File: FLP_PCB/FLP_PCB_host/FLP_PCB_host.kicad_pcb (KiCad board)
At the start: 2 copper layers, 90 x 90.5 mm, 91 parts, among them J3 GRPB052VWVN-RC, J4 OLED, J5 SMA-J-P-X-ST-TH1, Q1 Q_PMOS_DSG, Q2 UMH3N, U1 ESP32-WROOM-32E, U2 TPS61200DRC, U3 MCP73831-2-OT, U4 AMS1117-3.3, U5 CP2104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

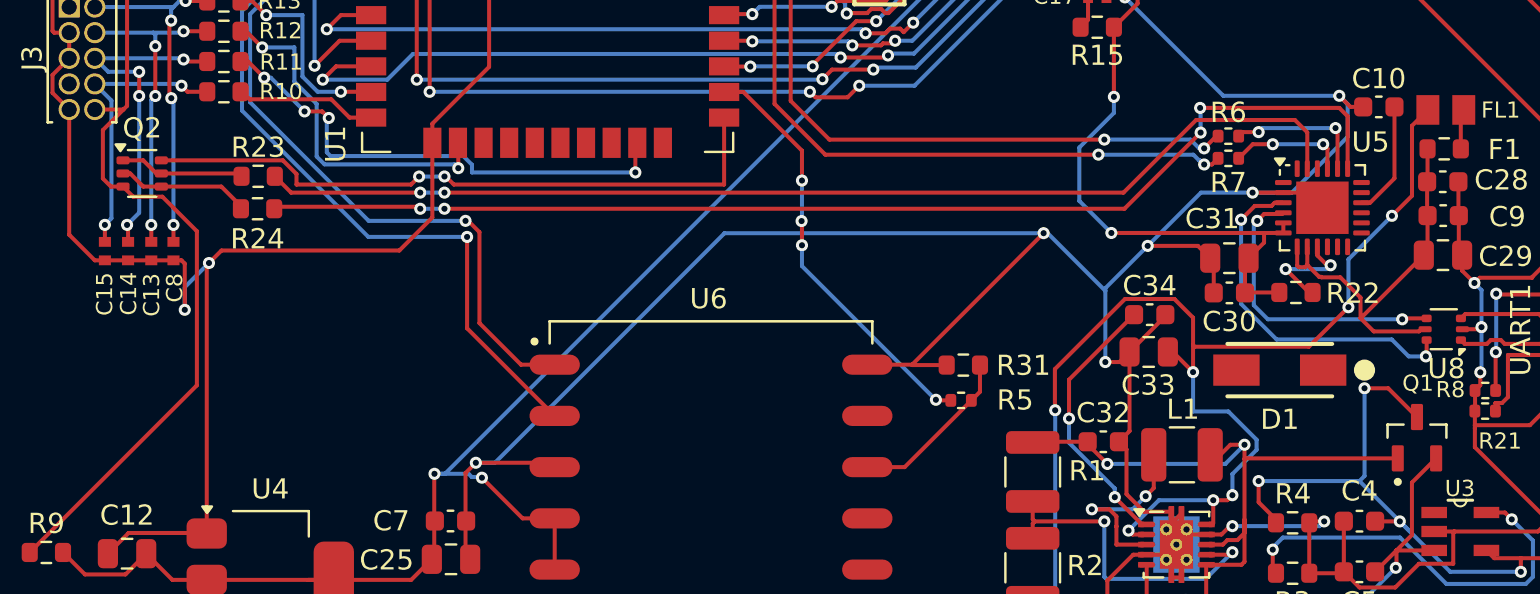
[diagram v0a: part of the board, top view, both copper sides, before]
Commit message: dir name change, host PCB finish
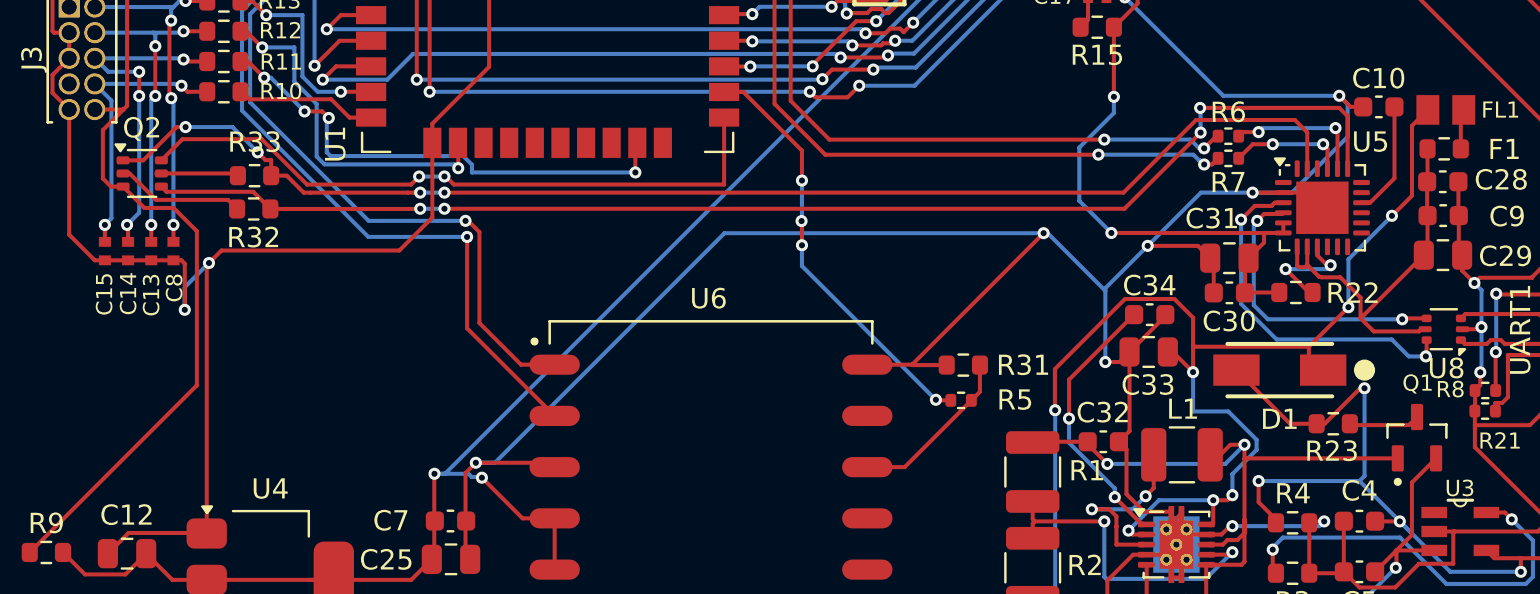
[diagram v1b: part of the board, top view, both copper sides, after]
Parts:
- removed R24: 10K, Resistor_SMD:R_0603_1608Metric
- added R32: 10K, Resistor_SMD:R_0603_1608Metric, F.Cu at (29.2, 59.0)
- added R33: 10K, Resistor_SMD:R_0603_1608Metric, F.Cu at (29.2, 57.4)
- Charger1: value Charger -> 10103594-0001LF
- F1: value Polyfuse -> 0603L100SLYR
- R23: value 10K -> 1K
- moved R23 54.7 mm to (82.7, 69.7)
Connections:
- D1 pad A: (no net) -> Net-(Charger1-VBUS)
- D1 pad C: (no net) -> 5v OUT
- Q1 pad 3: Net-(Charger1-VBUS) -> Net-(Q1-G)
- Q2 pad 2: RTS -> Net-(Q2A-B1)
- Q2 pad 5: DTR -> Net-(Q2B-B2)
- R23 pad 1: DTR -> Net-(Charger1-VBUS)
- R23 pad 2: Net-(U5-~{DTR}) -> Net-(Q1-G)
- U5 pad 19: Net-(U5-~{RTS}) -> RTS
- U5 pad 23: Net-(U5-~{DTR}) -> DTR
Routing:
- net Net-(U5-~{RTS}): track 58.8 -> 0.00 mm, vias 4 -> 0
- net DTR: track 6.20 -> 64.7 mm, vias 0 -> 4
- net RTS: track 6.56 -> 65.0 mm, vias 0 -> 4
- net Net-(U5-~{DTR}): track 55.1 -> 0.00 mm, vias 2 -> 0
- net Net-(Q2A-B1): track 0.00 -> 6.38 mm
- net Net-(Charger1-VBUS): track 33.9 -> 38.9 mm
- net Net-(Q2B-B2): track 0.00 -> 4.09 mm
- net Net-(Q1-G): track 0.00 -> 3.12 mm
- net 5v OUT: track 111.4 -> 112.9 mm
- net IO0: track 32.4 -> 32.9 mm

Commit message: modify
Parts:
- Y1: footprint Crystal:Crystal_SMD_2012-2Pin_2.0x1.2mm -> Crystal:Crystal_SMD_2016-4Pin_2.0x1.6mm
- moved Y1 0.79 mm to (70.4, 23.5)
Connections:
- D1 pad A: Net-(Charger1-VBUS) -> (no net)
- D1 pad C: 5v OUT -> (no net)
- Y1 pad 2: Net-(U7-XTA) -> 
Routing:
- net Net-(U7-XTA): track 5.06 -> 6.62 mm
- net GND: track 482.1 -> 483.1 mm

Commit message: PCB finish
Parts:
- turned C22 to 0 degrees
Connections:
- Y1 pad 2:  -> (no net)
- Y1 pad 4:  -> (no net)
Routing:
- net GND: track 483.1 -> 481.6 mm
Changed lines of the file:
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@@
 	(net 107 "unconnected-(U6-EX_ANT-Pad11)")
 	(net 108 "Net-(Q2A-B1)")
-	(net 109 "")
 	(footprint "Capacitor_SMD:C_0603_1608Metric"
 		(layer "F.Cu")
@@
 		(pad "" np_thru_hole circle
 			(at -2.89 -3.68 90)
-			(size 0.5 0.5)
-			(drill 0.5)
+			(size 0.65 0.65)
+			(drill 0.65)
 			(layers "*.Cu" "*.Mask")
 		)
 		(pad "" np_thru_hole circle
 			(at 2.89 -3.68 90)
-			(size 0.5 0.5)
-			(drill 0.5)
+			(size 0.65 0.65)
+			(drill 0.65)
 			(layers "*.Cu" "*.Mask")
 			(clearance 0.25)
@@
 		(pad "A1_B12" smd rect
 			(at -3.2 -4.75 90)
-			(size 0.6 1.14)
+			(size 0.6 0.98)
 			(layers "F.Cu" "F.Mask" "F.Paste")
-			(solder_mask_margin 0.09)
+			(solder_mask_margin 0.06)
 			(clearance 0.2)
 		)
 		(pad "A4_B9" smd rect
 			(at -2.4 -4.75 90)
-			(size 0.6 1.14)
+			(size 0.6 1)
 			(layers "F.Cu" "F.Mask" "F.Paste")
 			(solder_mask_margin 0.09)
@@
 		(pad "B1_A12" smd rect
 			(at 3.2 -4.75 90)
-			(size 0.6 1.14)
+			(size 0.6 0.98)
 			(layers "F.Cu" "F.Mask" "F.Paste")
 			(solder_mask_margin 0.09)
@@
 		(pad "B4_A9" smd rect
 			(at 2.4 -4.75 90)
-			(size 0.6 1.14)
+			(size 0.6 1)
 			(layers "F.Cu" "F.Mask" "F.Paste")
 			(solder_mask_margin 0.09)
@@
 			(size 0.9 0.8)
 			(layers "F.Cu" "F.Mask" "F.Paste")
-			(net 109 "")
 			(pinfunction "2")
 			(pintype "passive")
@@
 			(size 0.9 0.8)
 			(layers "F.Cu" "F.Mask" "F.Paste")
-			(net 109 "")
 		)
 		(embedded_fonts no)
@@
 	(footprint "Capacitor_SMD:C_0402_1005Metric"
 		(layer "F.Cu")
-		(at 71 20.6 180)
+		(at 71 20.6)
 		(descr "Capacitor SMD 0402 (1005 Metric), square (rectangular) end terminal, IPC_7351 nominal, (Body size source: IPC-SM-782 page 76, https://www.pcb-3d.com/wordpress/wp-content/uploads/ipc-sm-782a_amendment_1_and_2.pdf), generated with kicad-footprint-generator")
 		(tags "capacitor")
 		(property "Reference" "C22"
-			(at 0.45 1.4 0)
+			(at -0.55 -1.59 0)
 			(layer "F.SilkS")
 			(effects
@@
 		)
 		(property "Datasheet" ""
-			(at 0 0 180)
+			(at 0 0 0)
 			(unlocked yes)
 			(layer "F.Fab")
@@
 		)
 		(property "Description" "Unpolarized capacitor"
-			(at 0 0 180)
+			(at 0 0 0)
 			(unlocked yes)
 			(layer "F.Fab")
@@
 		(attr smd)
 		(fp_line
-			(start -0.107836 0.36)
-			(end 0.107836 0.36)
+			(start -0.107836 -0.36)
+			(end 0.107836 -0.36)
 			(stroke
 				(width 0.12)
@@
 		)
 		(fp_line
-			(start -0.107836 -0.36)
-			(end 0.107836 -0.36)
+			(start -0.107836 0.36)
+			(end 0.107836 0.36)
 			(stroke
 				(width 0.12)
@@
 		)
 		(fp_line
-			(start 0.91 0.46)
-			(end -0.91 0.46)
+			(start -0.91 -0.46)
+			(end 0.91 -0.46)
 			(stroke
 				(width 0.05)
@@
 		)
 		(fp_line
-			(start 0.91 -0.46)
-			(end 0.91 0.46)
+			(start -0.91 0.46)
+			(end -0.91 -0.46)
 			(stroke
 				(width 0.05)
@@
 		)
 		(fp_line
-			(start -0.91 0.46)
-			(end -0.91 -0.46)
+			(start 0.91 -0.46)
+			(end 0.91 0.46)
 			(stroke
 				(width 0.05)
@@
 		)
 		(fp_line
-			(start -0.91 -0.46)
-			(end 0.91 -0.46)
+			(start 0.91 0.46)
+			(end -0.91 0.46)
 			(stroke
 				(width 0.05)
@@
 		)
 		(fp_line
-			(start 0.5 0.25)
-			(end -0.5 0.25)
+			(start -0.5 -0.25)
+			(end 0.5 -0.25)
 			(stroke
 				(width 0.1)
@@
 		)
 		(fp_line
-			(start 0.5 -0.25)
-			(end 0.5 0.25)
+			(start -0.5 0.25)
+			(end -0.5 -0.25)
 			(stroke
 				(width 0.1)
@@
 		)
 		(fp_line
-			(start -0.5 0.25)
-			(end -0.5 -0.25)
+			(start 0.5 -0.25)
+			(end 0.5 0.25)
 			(stroke
 				(width 0.1)
@@
 		)
 		(fp_line
-			(start -0.5 -0.25)
-			(end 0.5 -0.25)
+			(start 0.5 0.25)
+			(end -0.5 0.25)
 			(stroke
 				(width 0.1)
@@
 		)
 		(pad "1" smd roundrect
-			(at -0.48 0 180)
+			(at -0.48 0)
 			(size 0.56 0.62)
 			(layers "F.Cu" "F.Mask" "F.Paste")
@@
 		)
 		(pad "2" smd roundrect
-			(at 0.48 0 180)
+			(at 0.48 0)
 			(size 0.56 0.62)
 			(layers "F.Cu" "F.Mask" "F.Paste")
@@
 	)
 	(segment
-		(start 69.926 21.964)
-		(end 69.926 22.054)
-		(width 0.2)
-		(layer "F.Cu")
-		(net 15)
-	)
-	(segment
 		(start 69.87 22.11)
 		(end 69.87 22.76)
@@
 	)
 	(segment
-		(start 69.926 22.054)
-		(end 69.87 22.11)
-		(width 0.2)
-		(layer "F.Cu")
-		(net 15)
-	)
-	(segment
-		(start 70.52 21.37)
-		(end 70.52 20.6)
-		(width 0.2)
-		(layer "F.Cu")
-		(net 15)
-	)
-	(segment
-		(start 69.971 22.009)
-		(end 69.926 21.964)
+		(start 70.116 21.964)
+		(end 71.48 20.6)
 		(width 0.2)
 		(layer "F.Cu")
@@
 	)
 	(segment
-		(start 69.926 21.964)
-		(end 70.52 21.37)
+		(start 69.87 22.11)
+		(end 69.971 22.009)
 		(width 0.2)
 		(layer "F.Cu")
@@
 	)
 	(segment
+		(start 68.82 21.36245)
+		(end 69.58245 20.6)
+		(width 0.2)
+		(layer "F.Cu")
+		(net 18)
+	)
+	(segment
 		(start 81.58 74.5)
 		(end 81.51 74.57)
@@
 	)
 	(segment
-		(start 70.869 19.989)
-		(end 71.48 20.6)
-		(width 0.2)
-		(layer "F.Cu")
-		(net 18)
-	)
-	(segment
 		(start 77.573932 74.735413)
 		(end 77.7 74.735413)
@@
 	)
 	(segment
-		(start 68.82 21.36245)
-		(end 70.19345 19.989)
-		(width 0.2)
-		(layer "F.Cu")
-		(net 18)
-	)
-	(segment
 		(start 79.95 21.05)
 		(end 80 21)
@@
 	)
 	(segment
-		(start 70.19345 19.989)
-		(end 70.869 19.989)
+		(start 69.58245 20.6)
+		(end 70.52 20.6)
 		(width 0.2)
 		(layer "F.Cu")
